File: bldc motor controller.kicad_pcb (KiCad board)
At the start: 4 copper layers, 26 x 26 mm, 50 parts, among them J1 Conn_01x04_Pin, M2 MountingHole_2.2mm_M2_DIN965_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, U1 C47023655, U3 C529358, U6 C126671

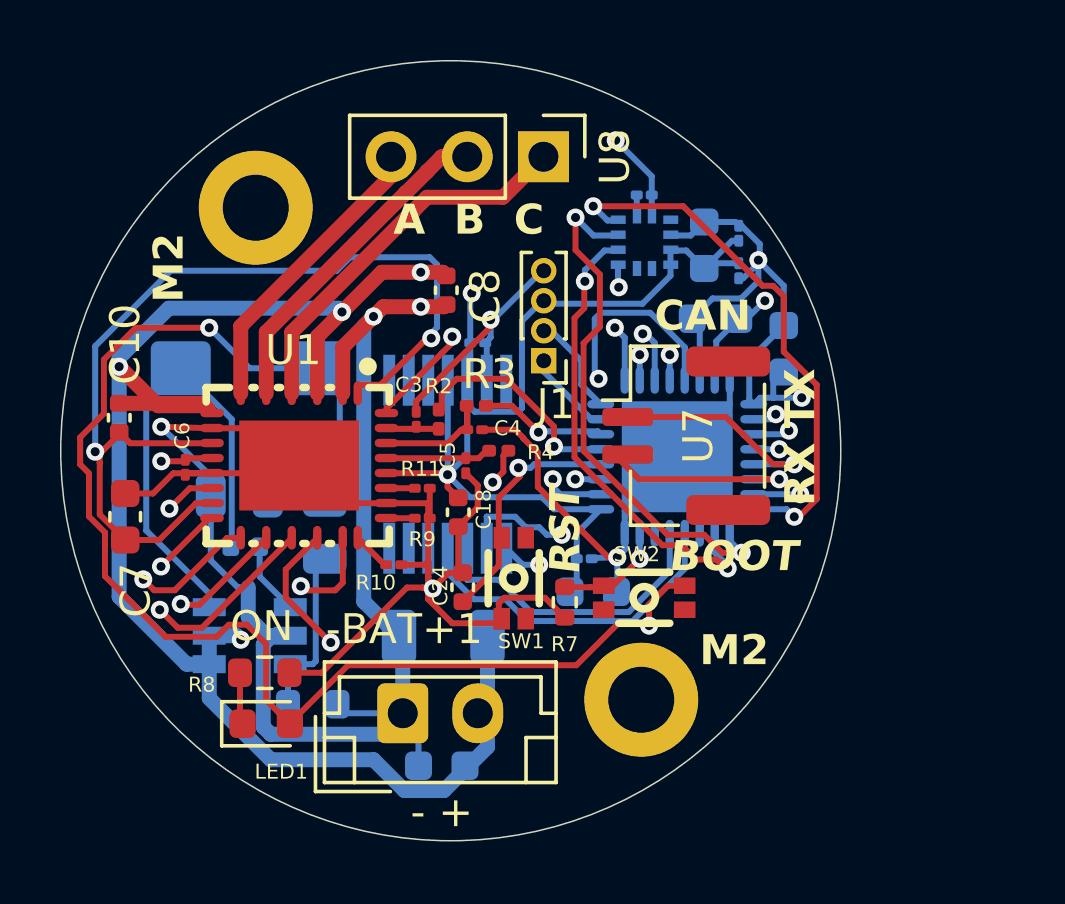
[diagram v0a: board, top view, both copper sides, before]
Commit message: Updated PCB, need to do some tweaks on motor controller schematic side
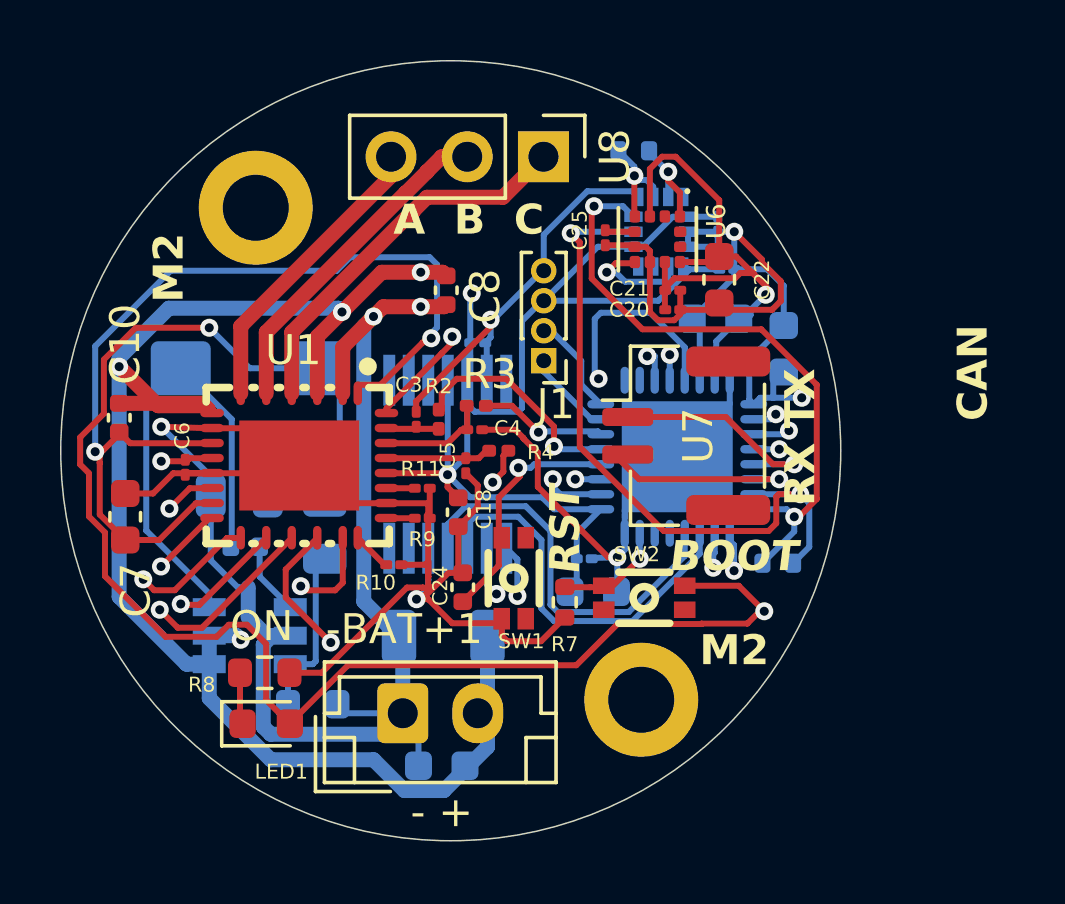
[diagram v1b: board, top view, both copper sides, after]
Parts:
- added C25: 220nf, Capacitor_SMD:C_01005_0402Metric, F.Cu at (147.7, 80.9)
- added C26: 100nF, Capacitor_SMD:C_01005_0402Metric, B.Cu at (151.4, 80.5)
- added R12: 10kOhm, Resistor_SMD:R_0402_1005Metric, B.Cu at (148.6, 78.0)
- added R5: 10kOhm, Resistor_SMD:R_0402_1005Metric, B.Cu at (153.4, 91.8)
- added U2: ISM330DHCXTR, bldc-motor-footprints:PQFN50P250X300X86-14N, B.Cu at (149.5, 80.7)
- C20: value 220nf -> 100nF; moved to F.Cu
- C21, C22: moved to F.Cu
- U6: value C126671 -> LIS2MDLTR; footprint bldc-motor-footprints:LGA-12_L2.0-W2.0-P0.50-BL -> bldc-motor-footprints:PQFN50P200X200X70-12N; moved to F.Cu
- moved C20 3.94 mm to (149.9, 83.3)
- moved C21 2.29 mm to (149.9, 82.7), turned to 0 degrees
- moved C23 1.26 mm to (151.7, 82.0), turned to 0 degrees
- moved C22 1.25 mm to (151.4, 82.3), turned to -90 degrees
- moved U6 0.44 mm to (149.4, 81.0), turned to -90 degrees
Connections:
- net TI_AGND renamed GND
- C12 pad 2: TI_VREF -> +3.3V
- C13 pad 2: TI_VREF -> +3.3V
- C14 pad 2: TI_VREF -> +3.3V
- C15 pad 2: TI_VREF -> +3.3V
- C16 pad 2: TI_VREF -> +3.3V
- C17 pad 2: TI_VREF -> +3.3V
- C18 pad 2: TI_VREF -> +3.3V
- C19 pad 1: TI_VREF -> +3.3V
- C2 pad 1: TI_VREF -> +3.3V
- C20 pad 1: Net-(U6-C1) -> +3.3V
- C21 pad 1: TI_VREF -> +3.3V
- C22 pad 1: TI_VREF -> +3.3V
- C23 pad 1: TI_VREF -> +3.3V
- J1 pad 3: TI_VREF -> +3.3V
- L1 pad 2: TI_VREF -> +3.3V
- LED1 pad 2: TI_VREF -> +3.3V
- R1 pad 1: TI_VREF -> +3.3V
- SW2 pad 3: TI_VREF -> +3.3V
- U1 pad 24: TI_VREF -> +3.3V
- U3 pad 1: TI_VREF -> +3.3V
- U3 pad 10: SCK1 -> unconnected-(U3-PA5-Pad10)
- U3 pad 15: TI_VREF -> +3.3V
- U3 pad 17: TI_VREF -> +3.3V
- U3 pad 25: ENAB_MAG -> NSS1
- U3 pad 26: ENAB_XL -> SCK1
- U3 pad 27: unconnected-(U3-PB4-Pad27) -> MISO1
- U3 pad 29: MISO1 -> unconnected-(U3-PB6-Pad29)
- U3 pad 9: NSS1 -> unconnected-(U3-PA4-Pad9)
- U5 pad 11: TI_VREF -> +3.3V
- U5 pad 12: TI_VREF -> +3.3V
- U6 pad 1: SCL1 -> MSCL
- U6 pad 10: TI_VREF -> +3.3V
- U6 pad 2: ENAB_XL -> unconnected-(U6-NC1-Pad2)
- U6 pad 3: ENAB_MAG -> +3.3V
- U6 pad 4: SDA1 -> MSDA
- U6 pad 7: unconnected-(U6-INT_MAG/DRDY-Pad7) -> MDRDY
- U6 pad 9: TI_VREF -> +3.3V
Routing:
- net +3.3V: track 0.00 -> 158.9 mm, vias 0 -> 6
- net TI_VREF: track 138.6 -> 0.00 mm, vias 6 -> 0
- net ENAB_MAG: track 17.2 -> 0.00 mm, vias 2 -> 0
- net ENAB_XL: track 15.7 -> 0.00 mm, vias 2 -> 0
- net GND: track 81.9 -> 96.4 mm, vias 6 -> 5
- net SCL1: track 13.5 -> 23.3 mm
- net SCK1: track 19.1 -> 10.4 mm
- net NSS1: track 15.8 -> 10.4 mm
- net MDRDY: track 0.00 -> 3.64 mm, vias 0 -> 1
- net MSDA: track 0.00 -> 3.54 mm, vias 0 -> 1
- net MSCL: track 0.00 -> 3.40 mm, vias 0 -> 1
- net MISO1: track 10.1 -> 13.0 mm
- net SDA1: track 18.3 -> 21.1 mm
- net MOSI1: track 11.3 -> 13.4 mm
- net TIM1_CH3: track 23.0 -> 25.0 mm
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
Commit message: Centered encoder sensor
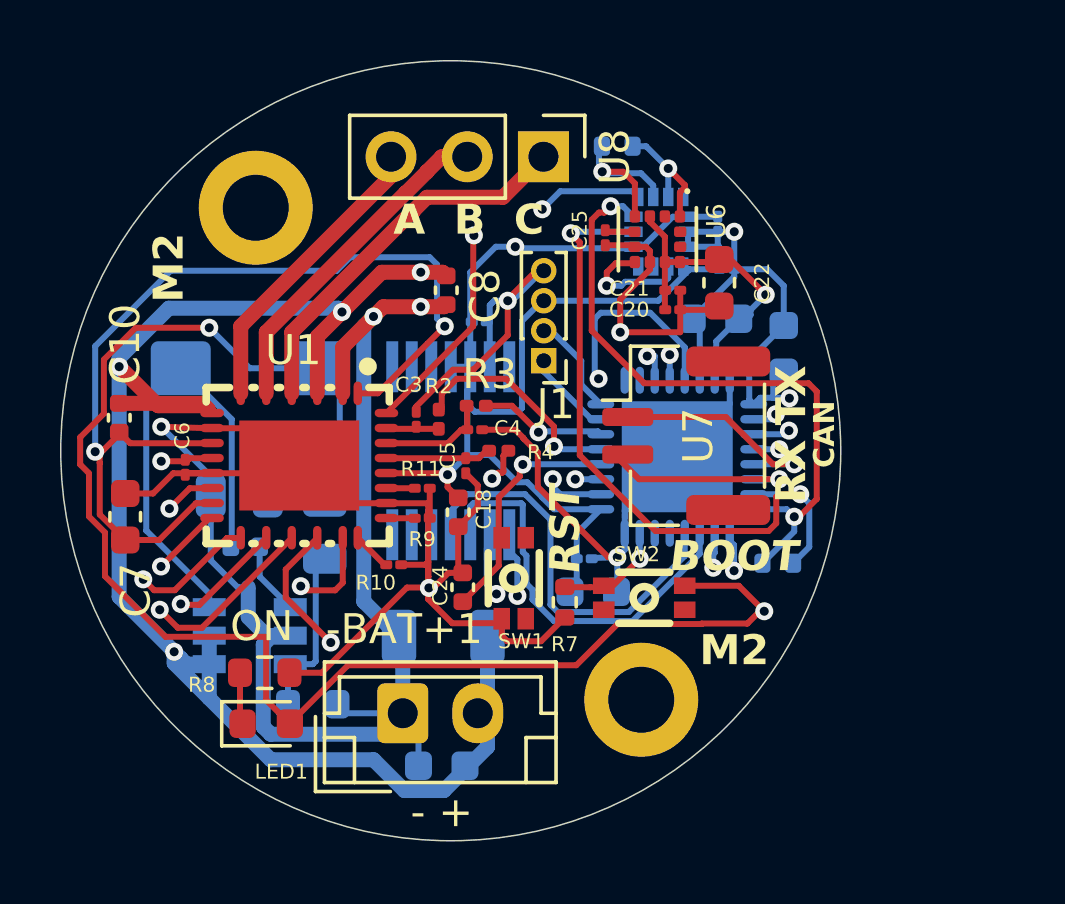
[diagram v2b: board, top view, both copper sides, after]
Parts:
- moved C19 0.70 mm to (143.4, 83.7)
- moved R12 0.57 mm to (148.1, 77.8)
- moved U5 0.46 mm to (142.5, 88.0)
- moved C22 0.10 mm to (151.4, 82.4)
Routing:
- net I-LIMIT: track 16.7 -> 24.1 mm
- net +3.3V: track 158.9 -> 152.4 mm
- net GND: track 96.4 -> 93.2 mm, vias 5 -> 7
- net MSDA: track 3.54 -> 5.46 mm
- net -BATT: track 49.1 -> 50.1 mm
- net MSCL: track 3.40 -> 4.45 mm
- net +BATT: track 85.4 -> 86.3 mm
- net SDA1: track 21.1 -> 21.8 mm

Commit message: Final push of the day
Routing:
- net +3.3V: track 152.4 -> 134.0 mm
- net I-LIMIT: track 24.1 -> 20.6 mm
- net GND: track 93.2 -> 92.1 mm
- net SCL1: track 23.3 -> 23.9 mm

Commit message: Wooo added a can transciever
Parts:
- added C27: 100 nf, Capacitor_SMD:C_01005_0402Metric, F.Cu at (153.7, 91.7)
- added U9: ~, bldc-motor-footprints:SON-8_L3.0-W3.0-P0.65-LS2.9-BL-EP, F.Cu at (150.8, 91.8)
- moved R7 3.30 mm to (146.8, 89.8), turned to 180 degrees
- moved SW2 2.45 mm to (146.5, 93.0), turned to 90 degrees
- moved R5 2.36 mm to (152.6, 94.0)
- moved C20 1.36 mm to (148.7, 82.7), turned to 180 degrees
- moved U7 0.81 mm to (150.2, 86.7)
- moved C22 0.70 mm to (151.5, 81.7)
- moved U8 0.55 mm to (145.0, 78.2)
- moved SW1 0.51 mm to (144.5, 92.8)
- moved C16 0.40 mm to (146.6, 91.6)
- moved C17 0.18 mm to (147.2, 92.9)
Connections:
- U3 pad 10: unconnected-(U3-PA5-Pad10) -> STB
- U3 pad 9: unconnected-(U3-PA4-Pad9) -> SHDN
- U7 pad 1: CAN_RX -> /C-
- U7 pad 2: CAN_TX -> /C+
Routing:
- net STB: track 0.00 -> 12.9 mm, vias 0 -> 1
- net SHDN: track 0.00 -> 8.61 mm, vias 0 -> 1
- net /C+: track 0.00 -> 6.50 mm
- net /C-: track 0.00 -> 6.16 mm
- net +3.3V: track 134.0 -> 139.9 mm, vias 6 -> 7
- net GND: track 92.1 -> 97.0 mm
- net TIM1_CH3N: track 14.9 -> 17.1 mm
- net TIM1_CH3: track 25.0 -> 23.0 mm
- net BOOT0: track 3.28 -> 4.93 mm
- net CAN_RX: track 8.00 -> 6.67 mm
- net MISO1: track 13.5 -> 14.8 mm
- net MOSI1: track 13.7 -> 14.7 mm
- net SCK1: track 10.4 -> 11.5 mm
- net NSS1: track 10.4 -> 11.4 mm
- net TIM1_CH2N: track 35.3 -> 36.3 mm
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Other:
- board text added: "CH CL"
- board text removed: "RX TX"

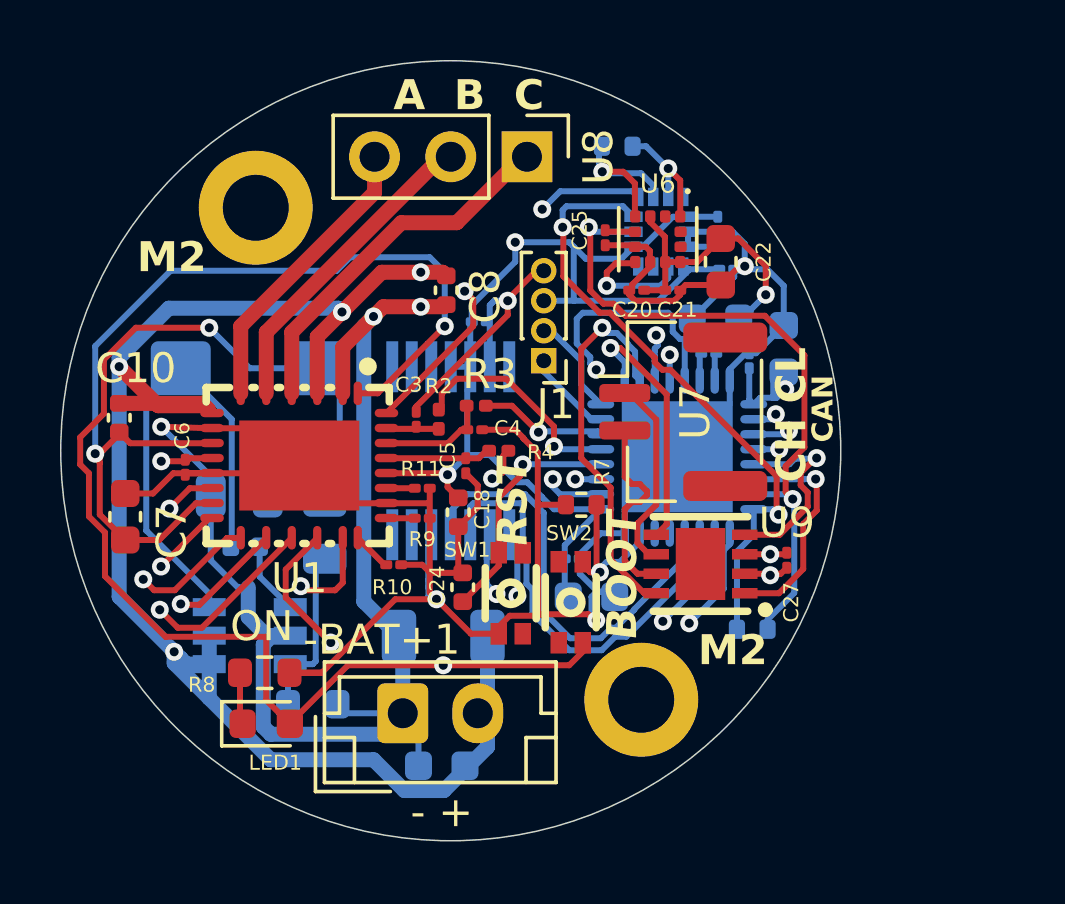
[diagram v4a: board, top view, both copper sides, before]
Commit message: Going to try to fix battery routing
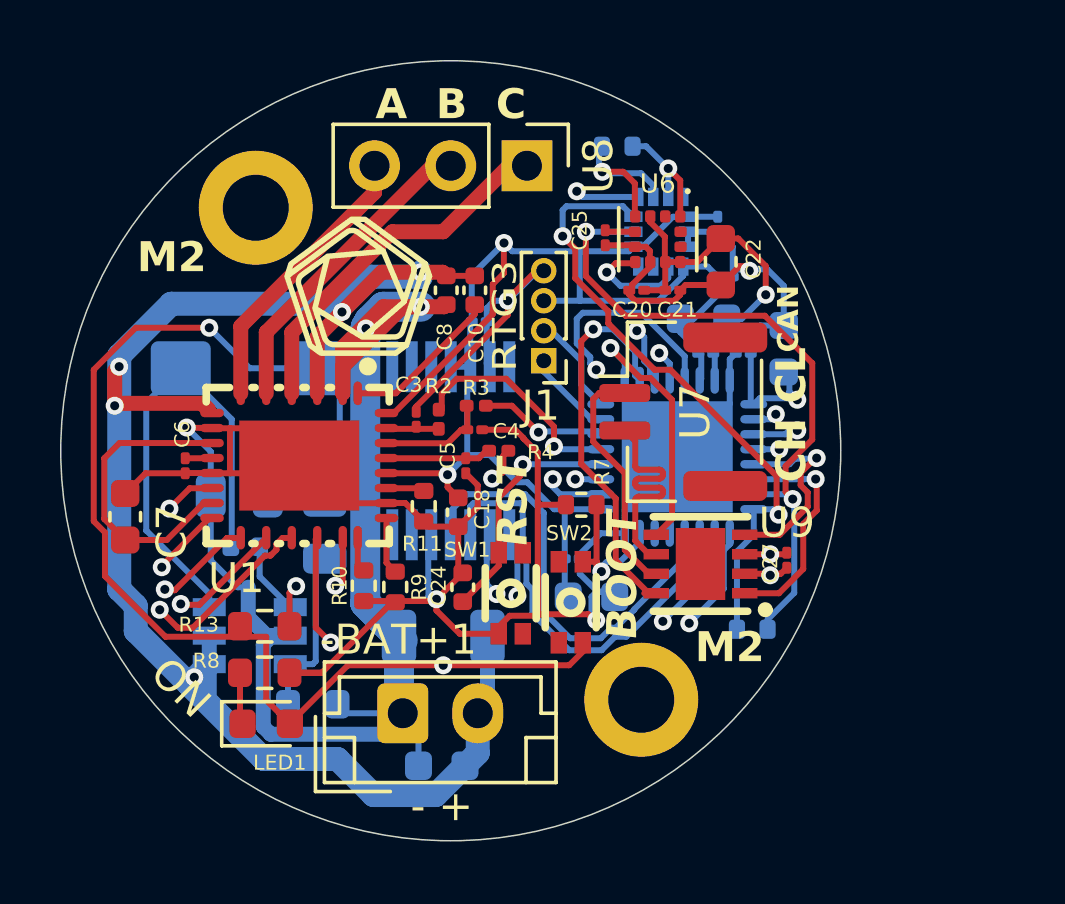
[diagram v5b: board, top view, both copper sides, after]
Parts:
- added R13: 5.1K, Resistor_SMD:R_0603_1608Metric, F.Cu at (136.3, 93.8)
- R10, R11, R9: value 2000 -> 3M; footprint Resistor_SMD:R_01005_0402Metric -> Resistor_SMD:R_0402_1005Metric
- moved C10 12.6 mm to (143.3, 82.7)
- moved R9 2.46 mm to (140.7, 92.5), turned to -90 degrees
- moved R10 1.22 mm to (139.6, 92.5), turned to -90 degrees
- moved R11 0.60 mm to (141.6, 89.8), turned to -90 degrees
- moved C13 0.40 mm to (150.9, 83.6)
- moved C14 0.32 mm to (152.2, 84.8), turned to 0 degrees
- moved U8 0.30 mm to (145.0, 78.5)
- moved C23 0.25 mm to (151.7, 82.2)
- moved C12 0.10 mm to (151.0, 84.8)
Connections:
- C10 pad 2: TI_AVDD -> Net-(U1-CP)
- C6 pad 2: I-LIMIT -> Net-(U1-GVDD)
- U1 pad 1: TI_AVDD -> Net-(U1-CP)
- U1 pad 10: I-LIMIT -> Net-(U1-GVDD)
- U1 pad 28: I-LIMIT -> +3.3V
- U7 pad 1: /C- -> /C+
- U7 pad 2: /C+ -> /C-
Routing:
- net TI_AVDD: track 33.4 -> 9.93 mm, vias 2 -> 0
- net I-LIMIT: track 20.4 -> 0.00 mm, vias 2 -> 0
- net +BATT: track 86.3 -> 98.6 mm, vias 4 -> 5
- net -BATT: track 50.1 -> 41.2 mm
- net TIM1_CH2: track 28.5 -> 36.0 mm
- net +3.3V: track 139.9 -> 145.8 mm
- net Net-(U1-CP): track 0.00 -> 5.31 mm
- net TIM1_CH3N: track 17.1 -> 21.6 mm
- net TIM1_CH1: track 27.0 -> 29.2 mm
- net TIM1_CH1N: track 27.3 -> 29.2 mm
- net TI_FAULT: track 19.2 -> 21.0 mm, vias 2 -> 3
- net /C-: track 6.16 -> 7.69 mm
- net /C+: track 6.50 -> 7.72 mm
- net Net-(U1-SDI/GAIN): track 0.94 -> 1.91 mm
- net TIM1_CH3: track 23.0 -> 22.2 mm
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- added copper zone on In2.Cu, net GND
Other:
- board text added: "M2"
- board text added: "RTG3"

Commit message: Re-routed power
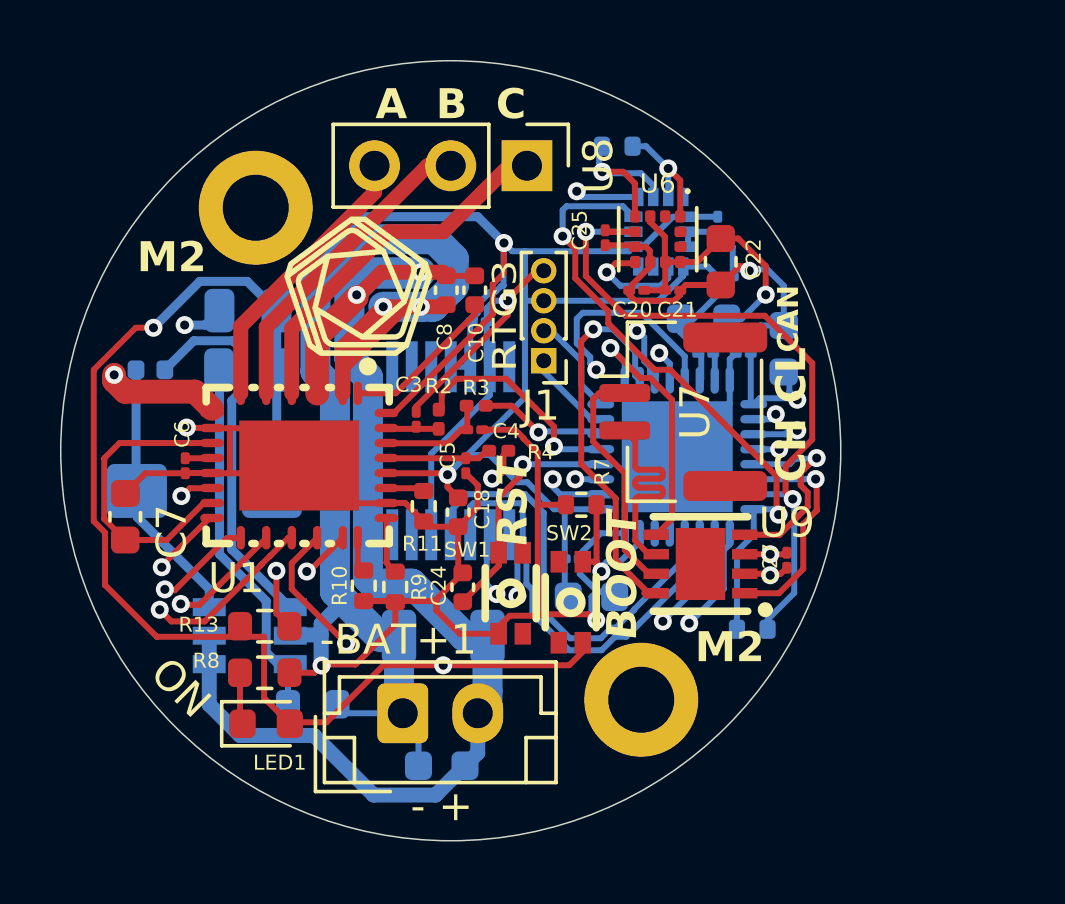
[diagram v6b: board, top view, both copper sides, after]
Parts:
- moved C11 6.69 mm to (132.5, 85.3)
- moved C2 6.18 mm to (135.7, 83.3)
- moved R1 5.93 mm to (135.7, 85.3), turned to 180 degrees
- moved L1 4.34 mm to (134.3, 89.3)
- moved NT1 2.90 mm to (138.2, 94.6), turned to -90 degrees
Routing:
- net +BATT: track 98.6 -> 57.4 mm, vias 5 -> 3
- net Net-(U4-CB): track 2.44 -> 12.6 mm
- net Net-(U4-FB): track 5.27 -> 12.2 mm
- net Net-(U4-SW): track 15.9 -> 9.09 mm
- net GND: track 96.3 -> 93.4 mm, vias 7 -> 8
- net +3.3V: track 145.8 -> 148.1 mm
- net TIM1_CH3N: track 21.6 -> 22.6 mm
- net TIM1_CH2: track 36.0 -> 35.2 mm

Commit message: updated to min capacitor size and increased width of 3.3v rail
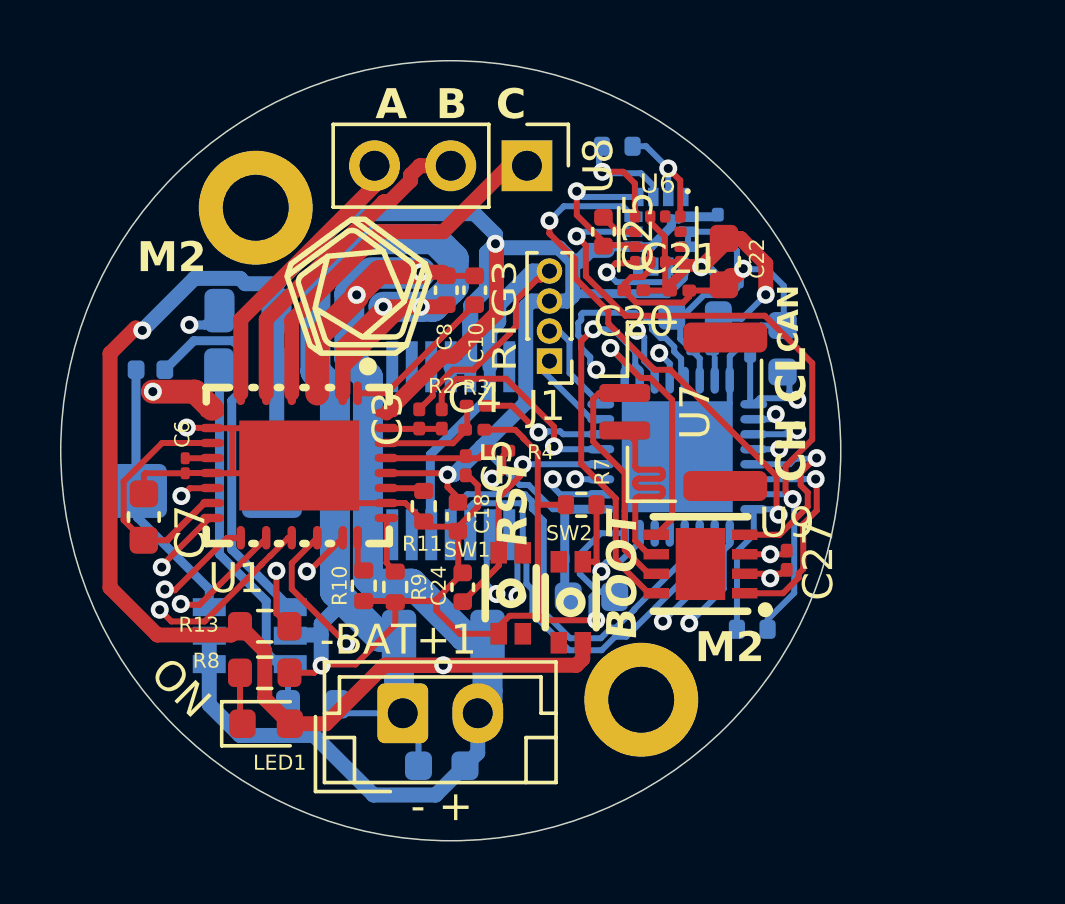
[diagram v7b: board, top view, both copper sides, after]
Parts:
- C12: value 10 nf -> 100 nf; footprint Capacitor_SMD:C_01005_0402Metric -> Capacitor_SMD:C_0201_0603Metric
- C14, C16, C19, C20, C21, C23, C26, C27, C3, C4, C5: footprint Capacitor_SMD:C_01005_0402Metric -> Capacitor_SMD:C_0201_0603Metric
- C25: footprint Capacitor_SMD:C_01005_0402Metric -> Capacitor_SMD:C_0402_1005Metric
- moved C7 0.62 mm to (132.3, 90.2)
- moved C14 0.33 mm to (152.5, 84.5), turned to -90 degrees
- moved C13 0.30 mm to (150.6, 83.5)
- moved C21 0.23 mm to (150.1, 82.7)
- moved C25 0.21 mm to (147.6, 80.7)
- moved C23 0.20 mm to (151.7, 82.4)
- moved J1 0.19 mm to (145.8, 85.0)
- moved C12 0.16 mm to (150.9, 84.6)
- moved C18 0.15 mm to (142.7, 90.2)
- moved C22 0.11 mm to (151.6, 81.7)
- moved C3 0.10 mm to (141.4, 86.9)
- moved R2 0.10 mm to (142.2, 86.9)
- moved C20 0.10 mm to (148.6, 82.7)
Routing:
- net +3.3V: track 148.1 -> 188.4 mm, vias 7 -> 8
- net GND: track 93.4 -> 97.6 mm, vias 8 -> 7
- net +BATT: track 57.4 -> 53.9 mm
- added copper zone on In1.Cu, net (none)
